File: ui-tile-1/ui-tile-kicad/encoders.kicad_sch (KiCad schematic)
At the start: 4 parts, among them SW3 EC11E15244G1, SW4 EC11E15244G1, SW5 EC11E15244G1, SW6 EC11E15244G1

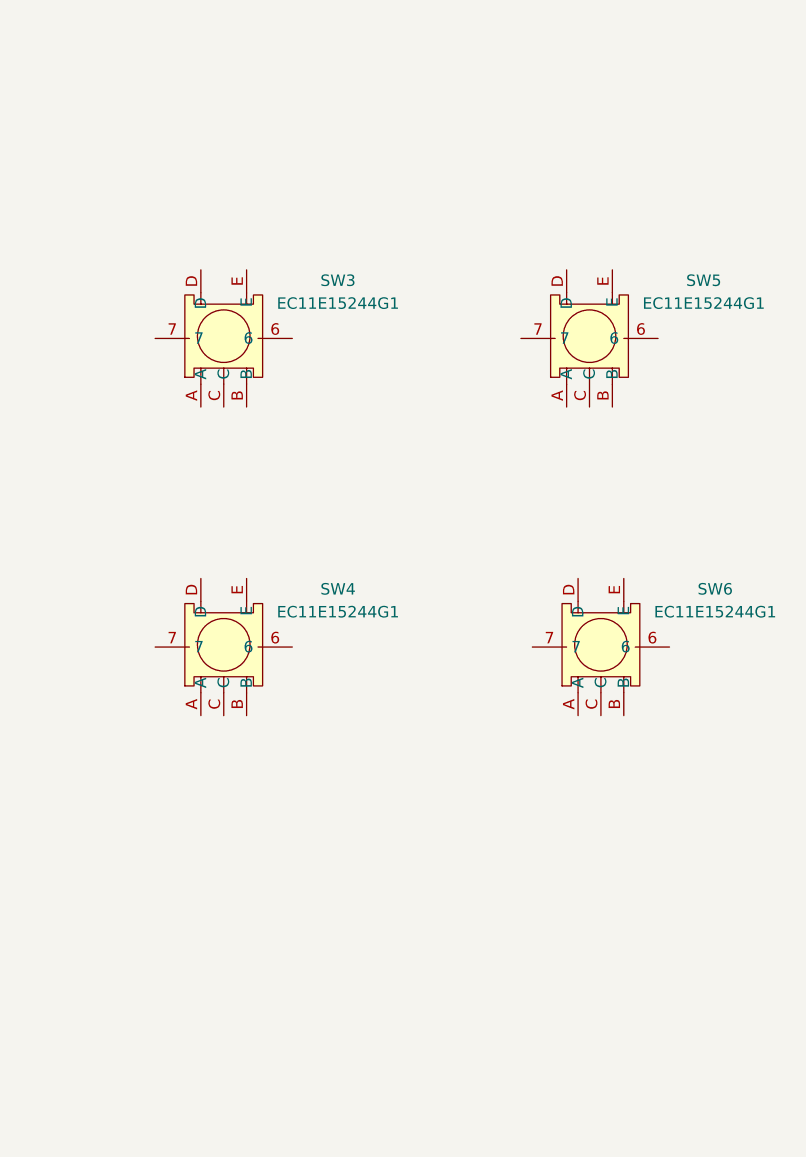
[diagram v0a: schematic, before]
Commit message: started on ws2812's
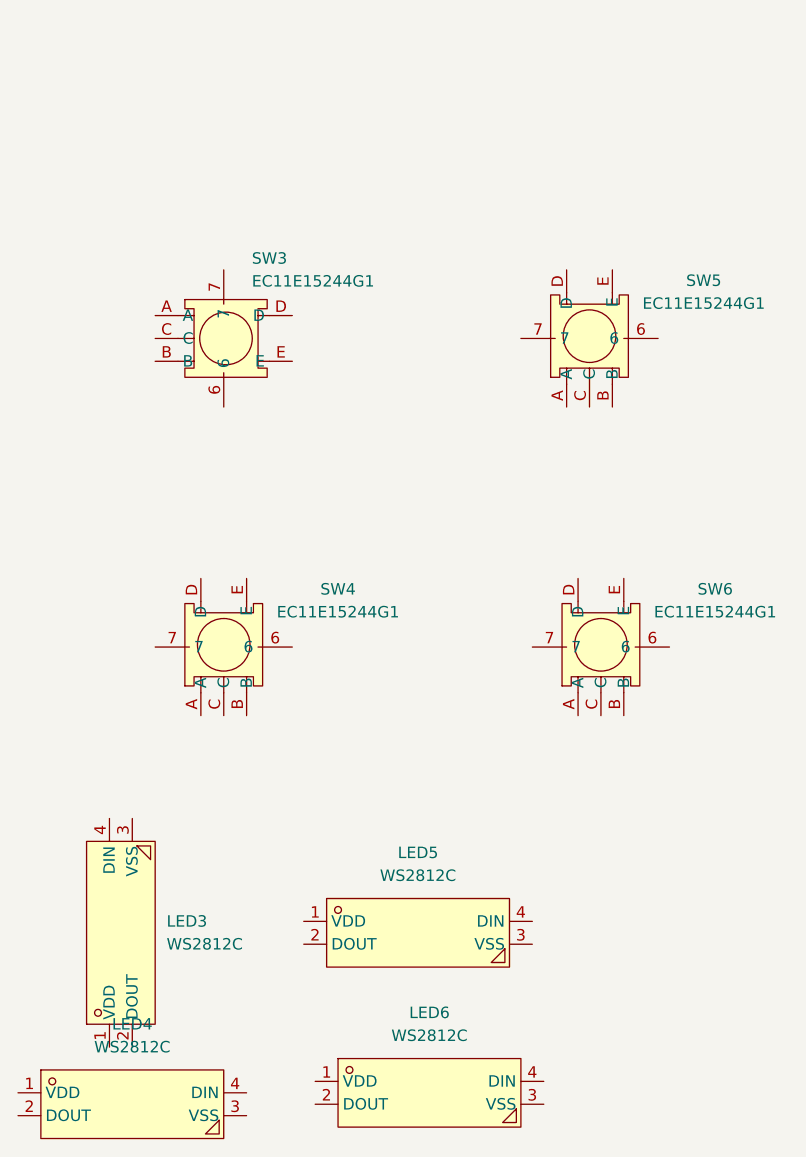
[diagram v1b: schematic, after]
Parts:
- added LED3, LED4, LED5, LED6: WS2812C, jlcpcb:LED-SMD_4P-L5.0-W5.0-LS5.4-TL-1, symbol jlcpcb:WS2812C
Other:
- moved on the sheet: SW3

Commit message: finished schematic electricals
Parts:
- removed LED3, LED4, LED5, LED6: WS2812C, jlcpcb:LED-SMD_4P-L5.0-W5.0-LS5.4-TL-1, symbol jlcpcb:WS2812C
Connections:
- net GND: now reaches SW5.6
- net GND: now also SW3.6, SW3.7, SW3.C, SW3.E, SW4.6, SW4.7, SW4.C, SW4.E, SW5.7, SW5.C, SW5.E, SW6.6, SW6.7, SW6.C, SW6.E
- net Enc3_A: now reaches SW5.A
- net Enc3_B: now reaches SW5.B
- net Enc3_SW: now reaches SW5.D
- net Enc4_A: now reaches SW6.A
- net Enc4_B: now reaches SW6.B
- net Enc4_SW: now reaches SW6.D
- net Enc1_A: now reaches SW3.A
- net Enc1_B: now reaches SW3.B
- net Enc1_SW: now reaches SW3.D
- net Enc2_A: now reaches SW4.A
- net Enc2_B: now reaches SW4.B
- net Enc2_SW: now reaches SW4.D
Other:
- moved on the sheet: SW3
